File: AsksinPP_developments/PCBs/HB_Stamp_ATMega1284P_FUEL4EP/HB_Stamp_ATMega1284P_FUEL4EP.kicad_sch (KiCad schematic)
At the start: 39 parts, among them J1 Power, J2 FTDI Debuger, J3 ISP Programmer, J4 I2C, J5 PA5/PCINT5, J6 PB3/AIN1/PCINT11, J7 PC4/PCINT20, U1 ATmega1284P-AU, U2 TPS61221DCK

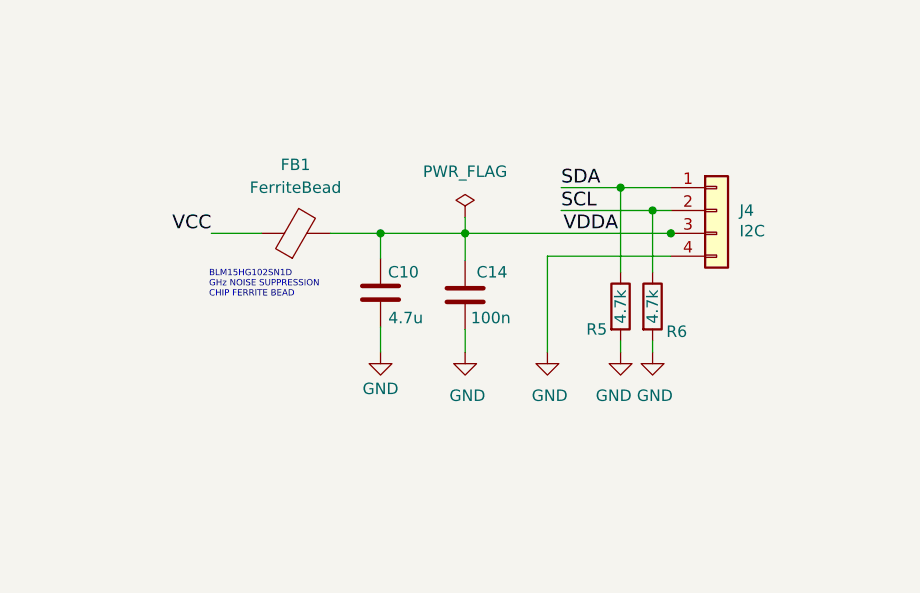
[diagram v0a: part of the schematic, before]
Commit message: PCBs: HB_Stamp_ATMega1284P_FUEL4EP and I2C_Module_SHT45_BME280_small_FUEL4EP: make I2C sockets fitting each other
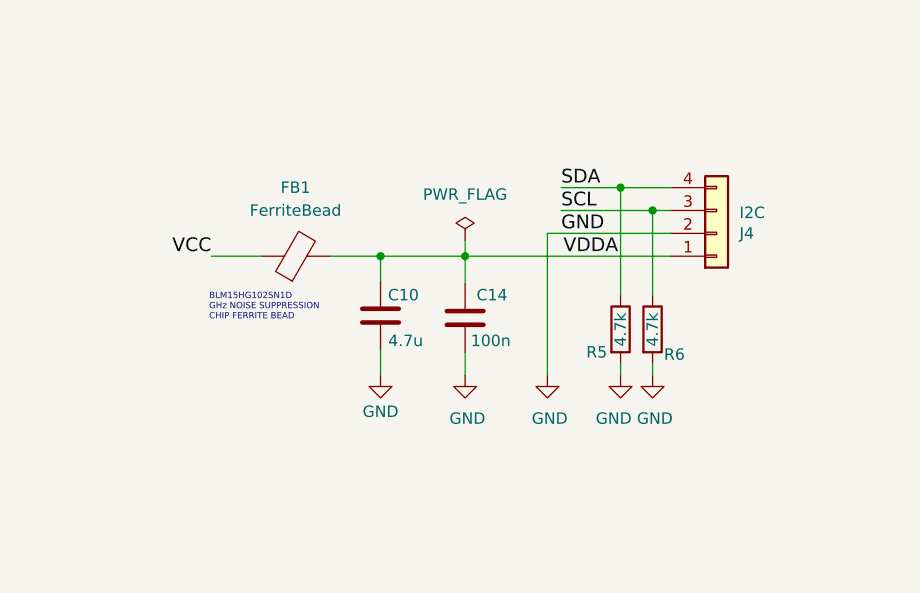
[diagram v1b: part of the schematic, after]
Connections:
- net GND: now also J4.2 (Pin_2); no longer J4.4 (Pin_4)
- net SCL: now also J4.3 (Pin_3); no longer J4.2 (Pin_2)
- net SDA: now also J4.4 (Pin_4); no longer J4.1 (Pin_1)
- net VDDA: now also J4.1 (Pin_1); no longer J4.3 (Pin_3)
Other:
- moved on the sheet: C10, C14, FB1, R5, R6

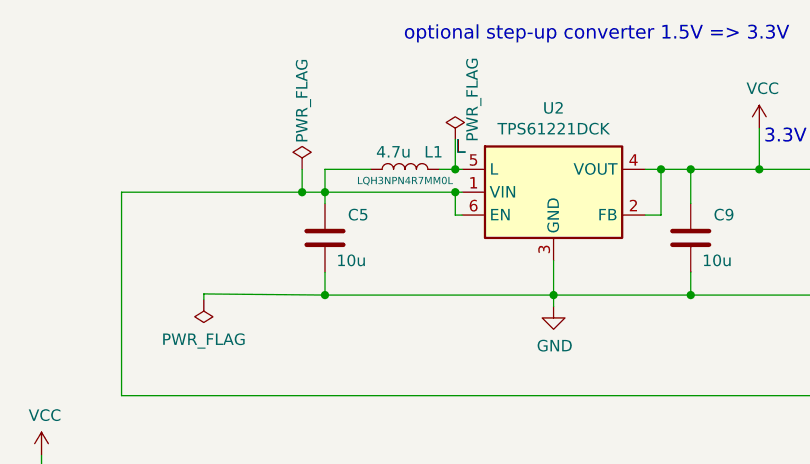
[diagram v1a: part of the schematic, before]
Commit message: PCBs: updates of HB_TH_Sensor_SHT45_AllInOne_FUEL4EP and HB_Stamp_ATMega1284P_FUEL4EP see README.mds
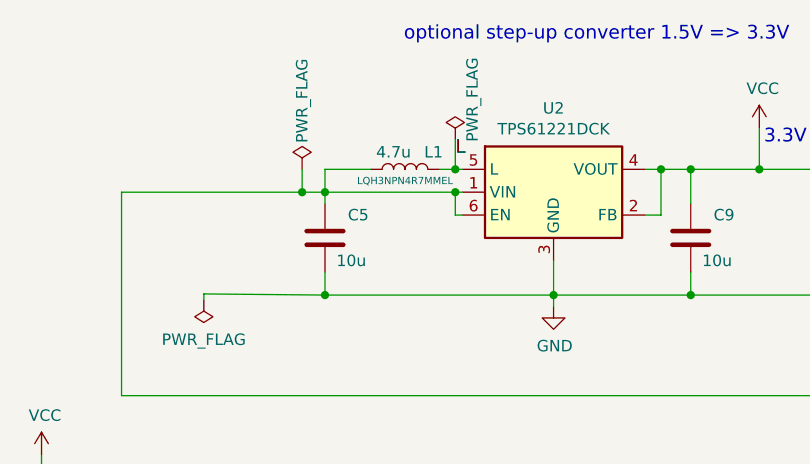
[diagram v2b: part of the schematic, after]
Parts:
- L1: LCSC C86077 -> C576538; Manufacturer Murata Electronics -> Murata; Productname LQH3NPN4R7MM0L -> LQH3NPN4R7MMEL; TYPE 0 -> 1212
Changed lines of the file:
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@@
   (title_block
     (title "HB_Stamp_ATMega1284P_FUEL4EP")
-    (date "2024-01-15")
-    (rev "1.1")
+    (date "2024-01-21")
+    (rev "1.2")
     (company "(C) FUEL4EP")
     (comment 1 "Creative Commons License, non-commercial")
@@
       (effects (font (size 1.27 1.27)) hide)
     )
-    (property "Datasheet" "https://datasheet.lcsc.com/lcsc/1810221721_Murata-Electronics-LQH3NPN4R7MM0L_C86077.pdf" (id 3) (at 107.188 30.48 0)
-      (effects (font (size 1.27 1.27)) hide)
-    )
-    (property "TYPE" "0" (id 4) (at 107.188 30.48 0)
-      (effects (font (size 1.27 1.27)) hide)
-    )
-    (property "LCSC" "C86077" (id 5) (at 110.363 28.575 0)
-      (effects (font (size 1.27 1.27)) hide)
-    )
-    (property "Manufacturer" "Murata Electronics" (id 6) (at 107.188 30.48 90)
+    (property "Datasheet" "https://datasheet.lcsc.com/lcsc/2304140030_Murata-Electronics-LQH3NPN4R7MMEL_C576538.pdf" (id 3) (at 107.188 30.48 0)
+      (effects (font (size 1.27 1.27)) hide)
+    )
+    (property "TYPE" "1212" (id 4) (at 107.188 30.48 0)
+      (effects (font (size 1.27 1.27)) hide)
+    )
+    (property "LCSC" "C576538" (id 5) (at 110.363 28.575 0)
+      (effects (font (size 1.27 1.27)) hide)
+    )
+    (property "Manufacturer" "Murata" (id 6) (at 107.188 30.48 90)
       (effects (font (size 1.524 1.524)) hide)
     )
-    (property "Productname" "LQH3NPN4R7MM0L" (id 7) (at 107.188 31.75 90)
+    (property "Productname" "LQH3NPN4R7MMEL" (id 7) (at 107.188 31.75 90)
       (effects (font (size 0.8 0.8)))
     )

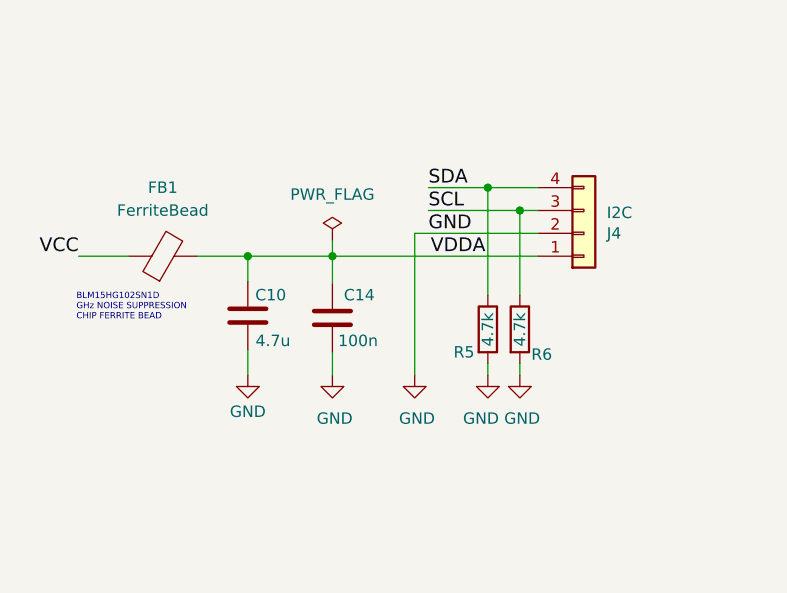
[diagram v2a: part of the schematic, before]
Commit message: PCBs: fix of I2C Pull-up resistors that were wrongly tied to GND
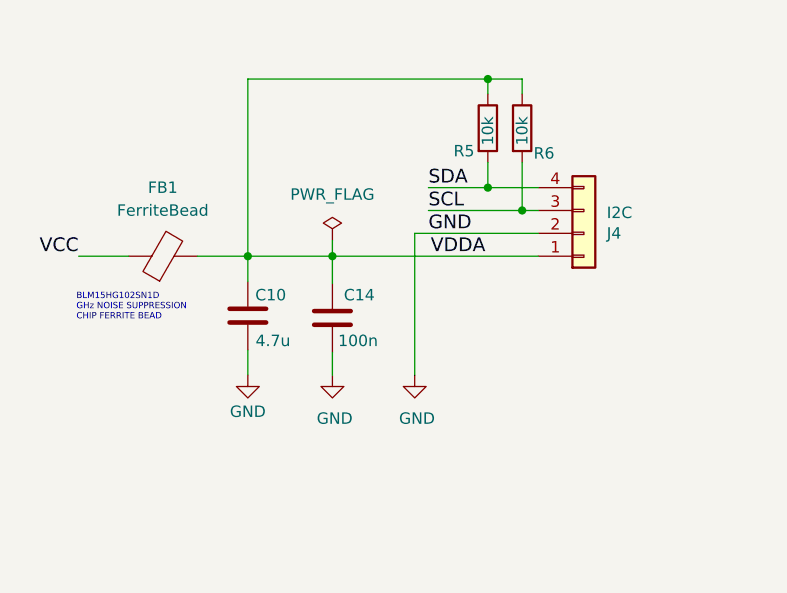
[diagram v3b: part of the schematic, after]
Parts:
- R5, R6: value 4.7k -> 10k; LCSC C25900 -> C25744
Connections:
- net GND: no longer R5.2, R6.2
- net SCL: now also R6.2; no longer R6.1
- net SDA: now also R5.2; no longer R5.1
- net VDDA: now also R5.1, R6.1
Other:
- moved on the sheet: R5, R6

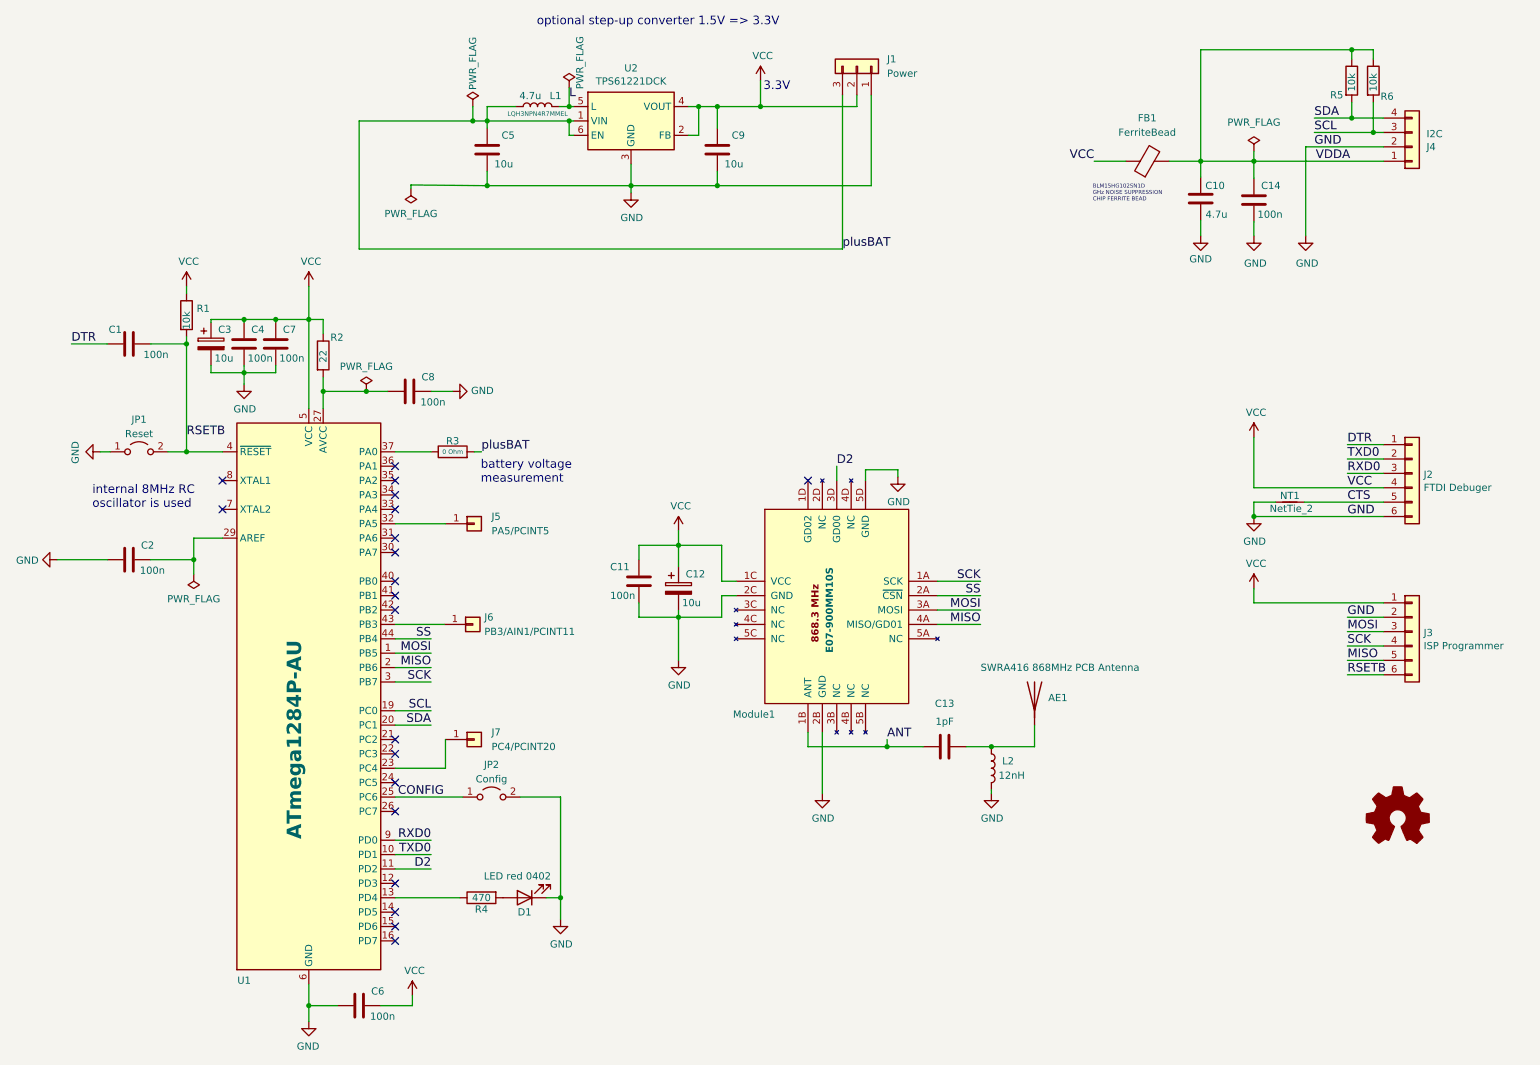
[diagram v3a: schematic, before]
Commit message: PCBs/HB_Stamp_ATMega1284P_FUEL4EP: migration to KiCAD 8
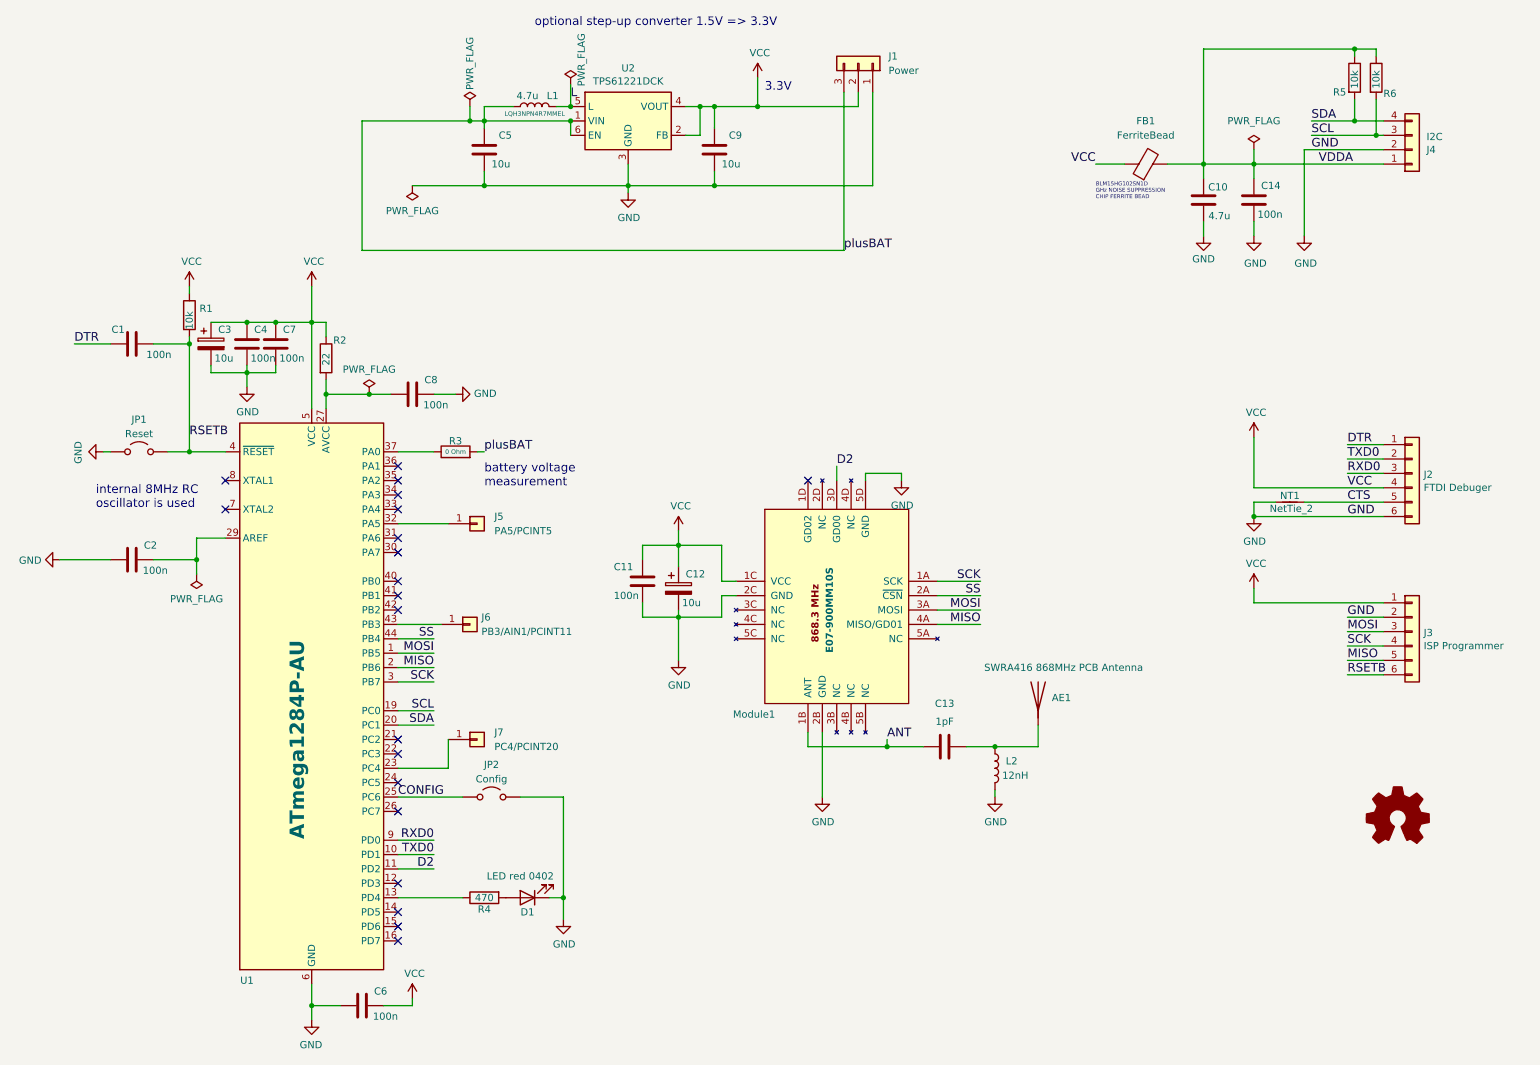
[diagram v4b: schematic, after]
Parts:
- AE1: footprint RF_Antenna:Texas_SWRA416_868MHz_915MHz -> FUEL4EP:Texas_SWRA416_868MHz_915MHz
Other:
- moved on the sheet: AE1, C1, C10, C11, C2, C4, C5, C6, C8, C9, D1, FB1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

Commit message: PCB updates
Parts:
- J1, J2, J3, J4, J5, J6, J7: now left out of the parts list
